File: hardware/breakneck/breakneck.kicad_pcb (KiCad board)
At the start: 2 copper layers, 53.3 x 64 mm, 109 parts, among them J1 CONN_EAST, J10 CONN_WEST, J12 GS2, J2 GS2, J3 CONN_01X02, J4 GS2, J5 USB_C_Rcpt_Min, J6 GS2, J7 CONN_OLED, J8 CONN_SOUTH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

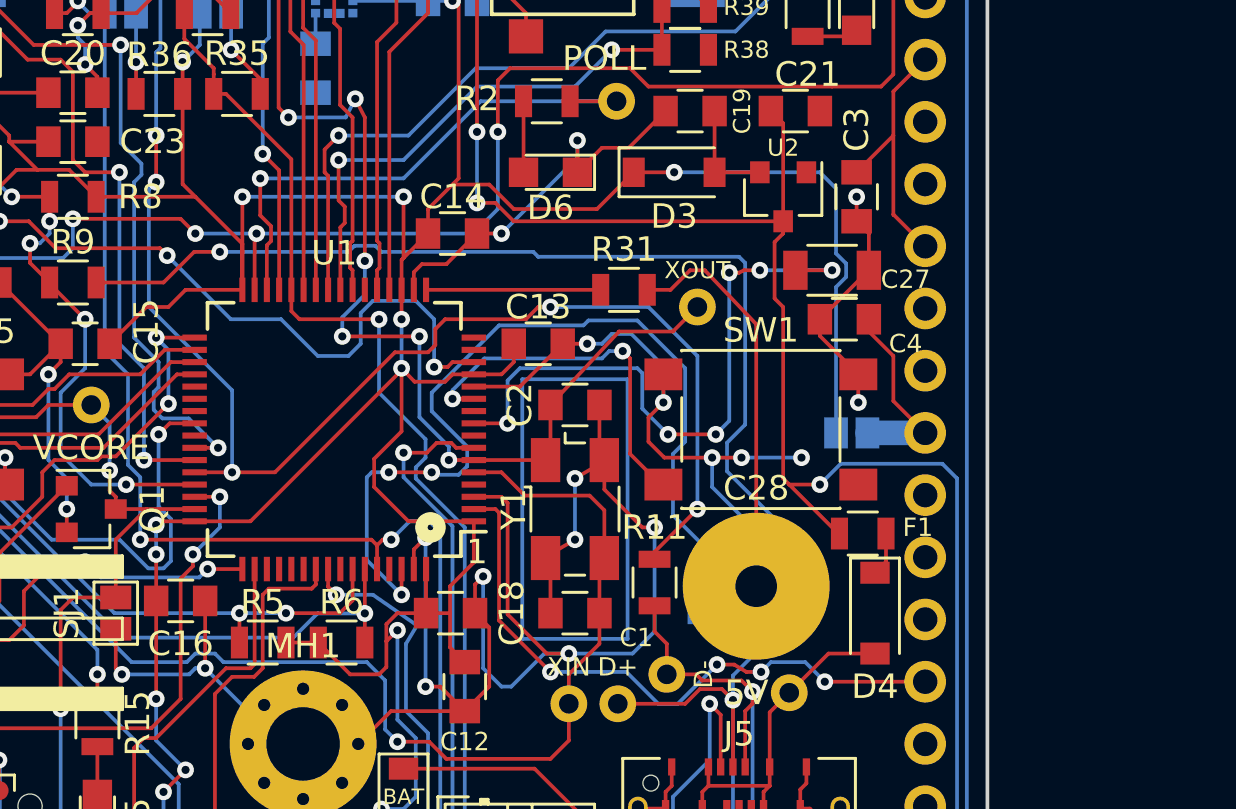
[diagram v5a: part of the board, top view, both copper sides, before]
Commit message: Added a second (32K for STM32L USB) crystal Y2 with provisional layout.
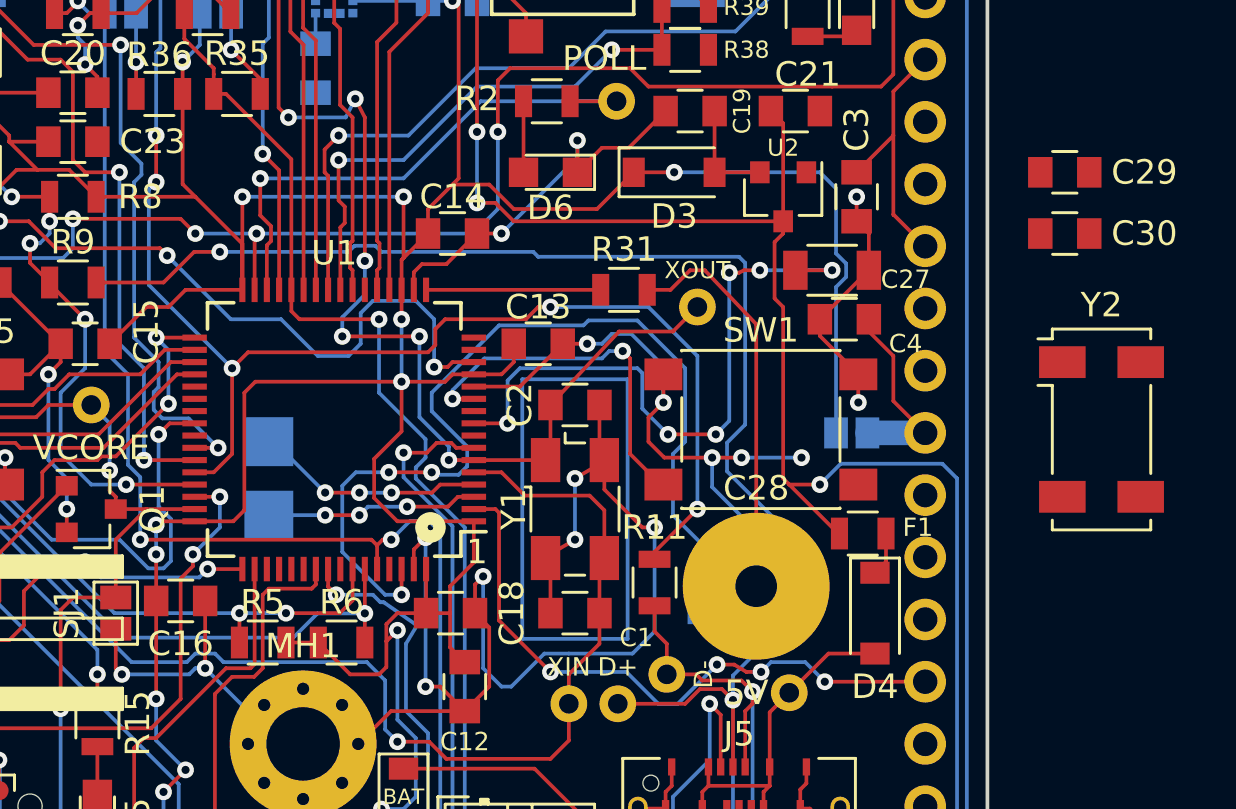
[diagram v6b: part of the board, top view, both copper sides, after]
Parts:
- added C29: 4.3pF, Monero_Local:C_0805, F.Cu at (156.5, 94.5)
- added C30: 4.3pF, Monero_Local:C_0805, F.Cu at (156.5, 97.0)
- added REF7: TestPoint_Pad_2.0x2.0mm, Monero_Local:TestPoint_Pad_2.0x2.0mm, B.Cu at (124.0, 105.5)
- added REF8: TestPoint_Pad_2.0x2.0mm, Monero_Local:TestPoint_Pad_2.0x2.0mm, B.Cu at (124.0, 108.5)
- added Y2: Crystal, Monero_Local:Crystal_SMD_Abracon_ABS25-4Pin_8.0x3.8mm, F.Cu at (158.0, 105.0)
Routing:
- net Net-(C30-Pad1): track 0.00 -> 9.37 mm, vias 0 -> 3
- net GND: track 244.4 -> 235.2 mm, vias 33 -> 32
- net Net-(C29-Pad1): track 0.00 -> 8.68 mm, vias 0 -> 3
- net +3V3: track 283.8 -> 286.4 mm
- net /USB_N: track 84.1 -> 81.9 mm
- net /CTLED: track 35.7 -> 37.3 mm

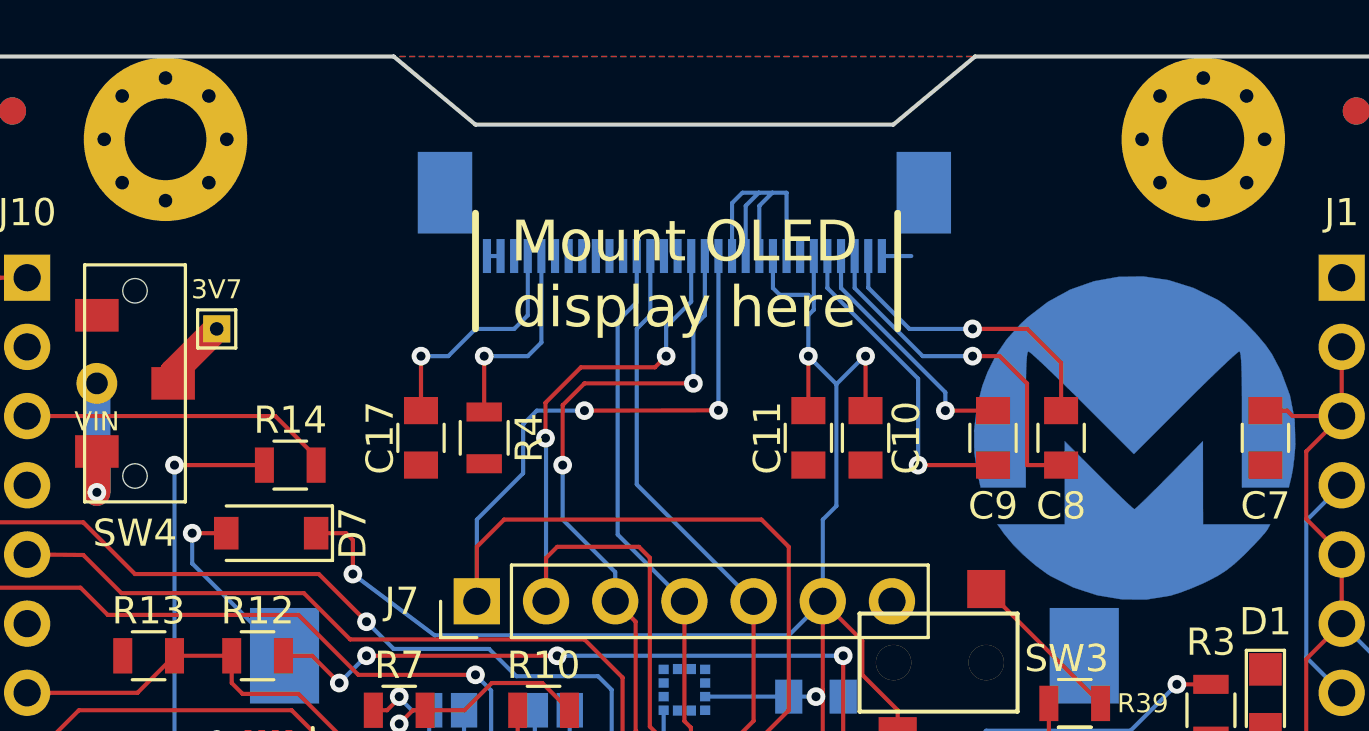
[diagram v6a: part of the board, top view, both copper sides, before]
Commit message: Added second display connector for 24-pin variants.
This change integrates reference designs intended for 30-pin connectors
as found in download/interfacing/ER-OLED0.96_Series_Interfacing.pdf
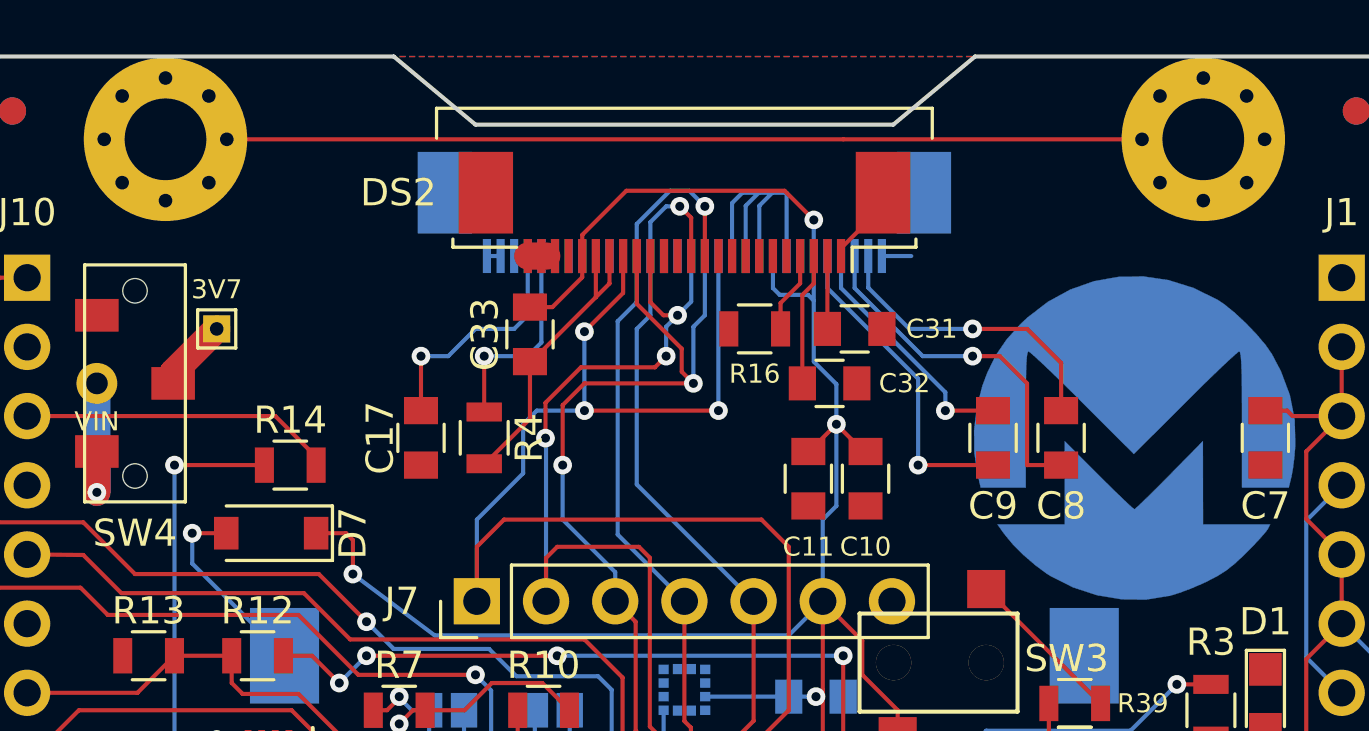
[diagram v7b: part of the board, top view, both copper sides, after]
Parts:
- added C31: 2.2uF, Monero_Local:C_0805, F.Cu at (132.9, 74.0)
- added C32: 4.7uF, Monero_Local:C_0805, F.Cu at (132.0, 76.0)
- added C33: 1uF, Monero_Local:C_0805, F.Cu at (121.0, 74.2)
- added DS2: ER-CON24, Monero_Local:Eastrising_ER-CON24HT-1_01x24_P0.50mm, F.Cu at (126.7, 70.5)
- added R16: 390K, Monero_Local:R_0805, F.Cu at (129.2, 74.0)
- moved C10 1.50 mm to (133.3, 79.5)
- moved C11 1.50 mm to (131.2, 79.5)
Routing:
- net GND: track 235.2 -> 288.0 mm
- net +3V3: track 286.4 -> 298.4 mm
- net /OLED_~CS~: track 52.5 -> 58.8 mm, vias 2 -> 3
- net /OLED_D1: track 29.7 -> 35.9 mm, vias 0 -> 1
- net /OLED_~RES~: track 33.8 -> 39.4 mm
- net Net-(C32-Pad1): track 0.00 -> 4.85 mm
- net /OLED_D0: track 30.4 -> 34.9 mm, vias 0 -> 1
- net Net-(DS2-Pad21): track 0.00 -> 2.97 mm
- net /OLED_DC: track 39.3 -> 42.2 mm, vias 2 -> 3
- net Net-(C31-Pad1): track 0.00 -> 2.67 mm
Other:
- board text removed: "Mount OLED display here"

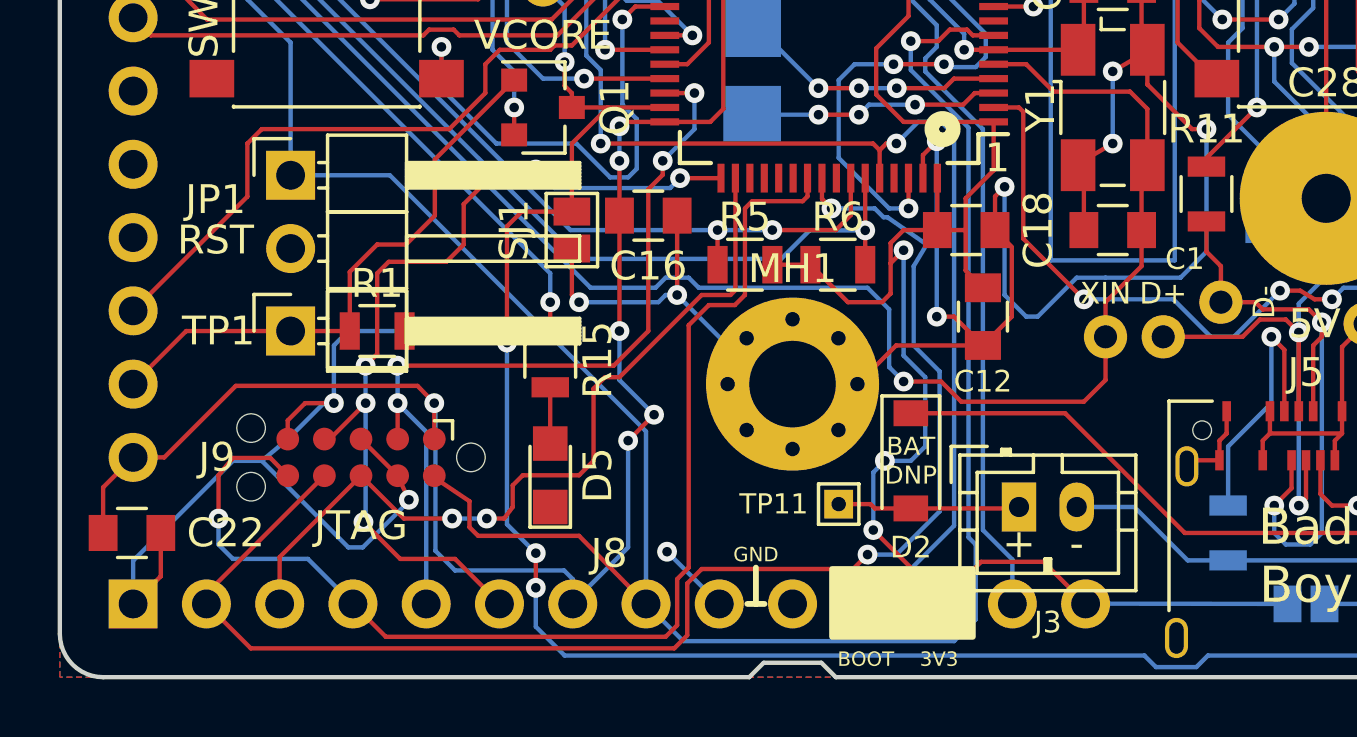
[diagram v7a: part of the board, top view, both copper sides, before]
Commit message: Integrated a MCP73831 controlled lithium ion battery charger layout.
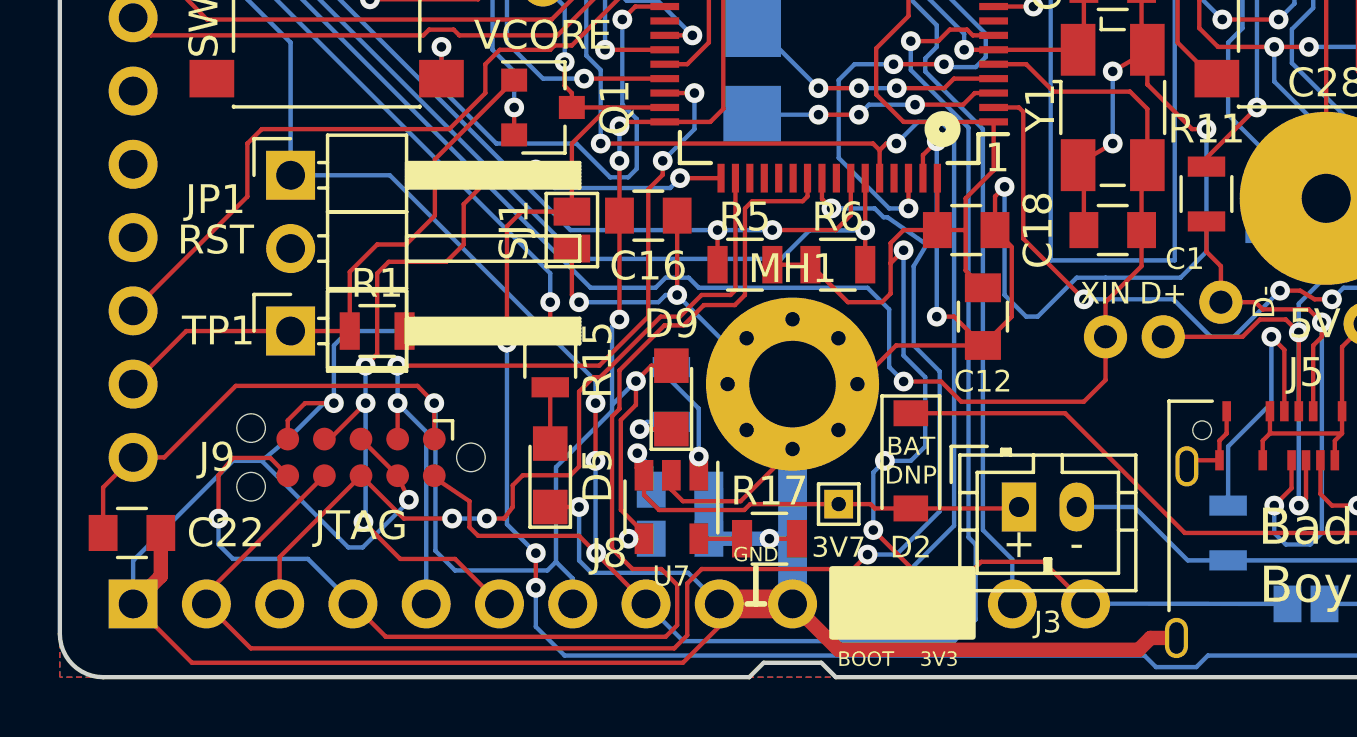
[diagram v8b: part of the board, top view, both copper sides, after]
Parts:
- added C34: 4.7uF, Monero_Local:C_0805, B.Cu at (121.5, 123.2)
- added C35: 4.7uF, Monero_Local:C_0805, B.Cu at (121.5, 121.5)
- added D9: LED, Monero_Local:LED_0805, F.Cu at (121.2, 118.3)
- added R17: 2K, Monero_Local:R_0805, F.Cu at (124.6, 123.2)
- added R18: 470, Monero_Local:R_0805, B.Cu at (121.2, 118.2)
- added U7: MCP73831-2-OT, Monero_Local:SOT-23-5, F.Cu at (121.2, 122.1)
- renumbered TP11 to 3V7
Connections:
- J3 pad 1: Net-(J3-Pad1) -> Net-(C35-Pad1)
- SW4 pad 3: Net-(J3-Pad1) -> Net-(C35-Pad1)
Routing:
- net GND: track 288.0 -> 354.0 mm, vias 32 -> 33
- net Net-(C35-Pad1): track 0.00 -> 10.1 mm, vias 0 -> 1
- net +3V3: track 298.4 -> 306.4 mm
- net Net-(R18-Pad1): track 0.00 -> 4.14 mm, vias 0 -> 1
- net /JTAG_TDO: track 41.7 -> 44.6 mm
- net /RESET: track 85.1 -> 82.6 mm, vias 2 -> 5
- net Net-(D9-Pad1): track 0.00 -> 2.30 mm, vias 0 -> 1
- net Net-(R17-Pad1): track 0.00 -> 1.50 mm
